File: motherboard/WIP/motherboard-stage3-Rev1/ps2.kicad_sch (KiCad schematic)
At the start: 12 parts, among them U9 ATmega88, Y3 32.768kHz

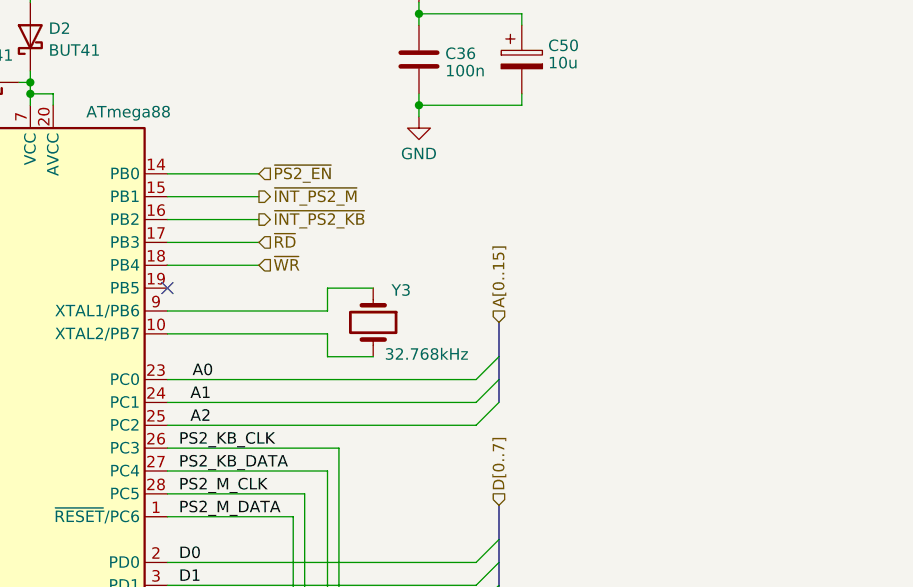
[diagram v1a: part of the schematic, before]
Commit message: Added Support for protected mode, routed R/W thru logic to amplify.
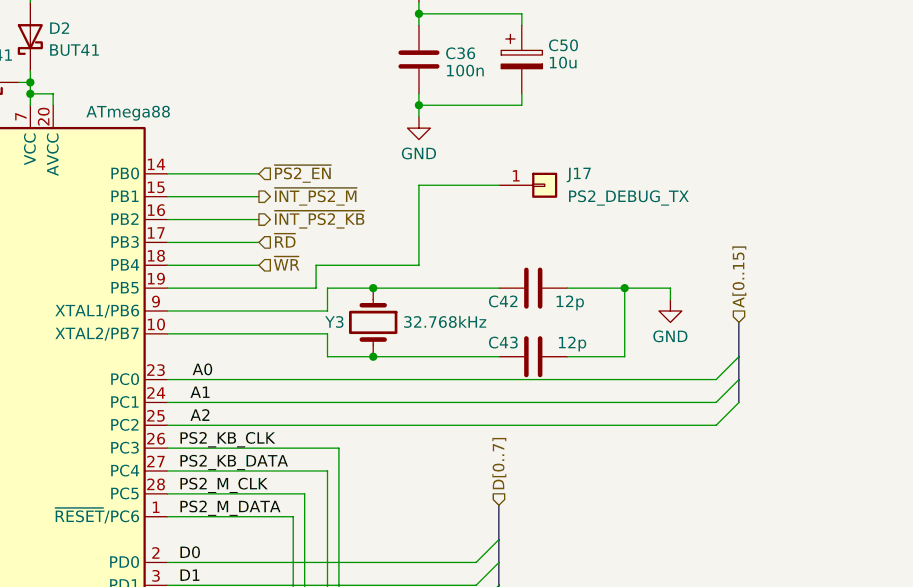
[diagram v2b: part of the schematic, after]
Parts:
- added C42, C43: 12p, Capacitor_THT:C_Disc_D5.0mm_W2.5mm_P2.50mm, symbol Device:C
- added J17: PS2_DEBUG_TX, Connector_PinHeader_2.54mm:PinHeader_1x01_P2.54mm_Vertical, symbol Connector_Generic:Conn_01x01
- U9: footprint Package_DIP:DIP-28_W7.62mm -> Package_DIP:DIP-28_W7.62mm_Socket
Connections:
- net GND: now also C42.2, C43.2
- net at U9.10 (XTAL2/PB7), Y3.2: now also C43.1
- net at U9.19 (PB5): now also J17.1 (Pin_1)
- net at U9.9 (XTAL1/PB6), Y3.1: now also C42.1
- no-connect marks 3 -> 2
